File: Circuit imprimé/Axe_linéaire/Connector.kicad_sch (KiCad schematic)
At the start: 2 parts, among them J1 Conn_01x14_Shielded

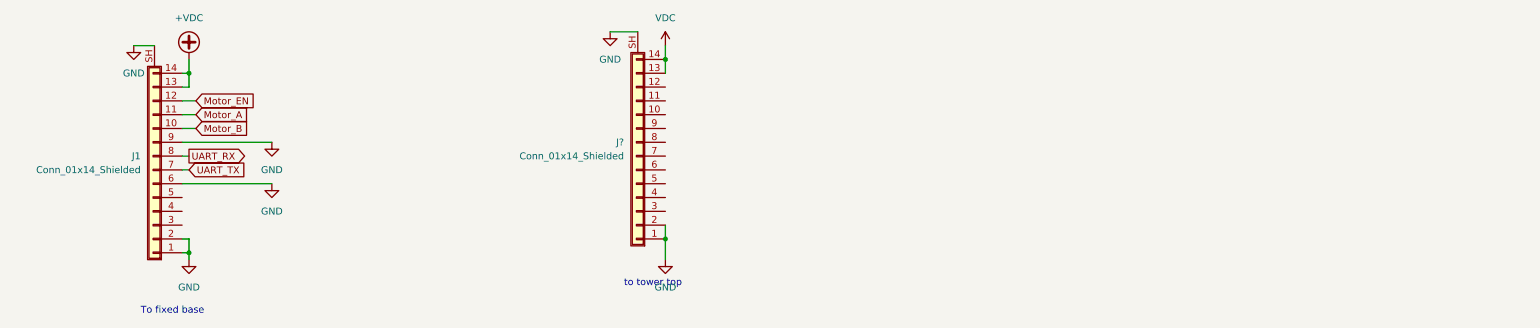
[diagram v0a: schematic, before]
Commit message: ajout du circuit de position + carte SD
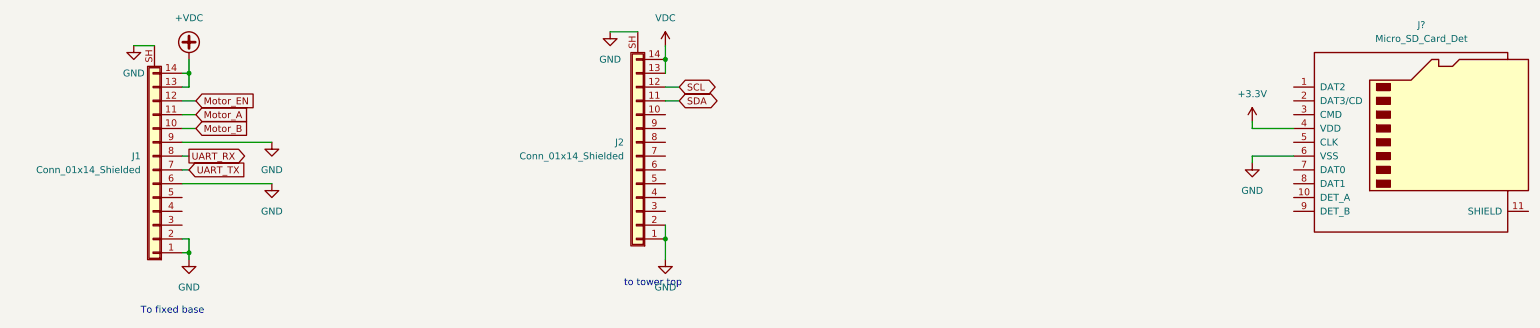
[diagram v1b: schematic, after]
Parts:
- added J?: Micro_SD_Card_Det, symbol Connector:Micro_SD_Card_Det
- gave numbers to parts that had none: 1
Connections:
- net GND: now also J?.6 (VSS)
- net SDA: now reaches J2.11 (Pin_11)
- net SCL: now reaches J2.12 (Pin_12)
- new net +3.3V: J?.4 (VDD)
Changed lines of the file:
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@@
+    (stroke (width 0) (type default) (color 0 0 0 0))
+  )
+  (wire (pts (xy 115.57 27.94) (xy 118.11 27.94))
+    (stroke (width 0) (type default) (color 0 0 0 0))
+  )
+  (wire (pts (xy 223.52 39.37) (xy 223.52 38.1))
     (stroke (width 0) (type default) (color 0 0 0 0))
   )
@@
     (stroke (width 0) (type default) (color 0 0 0 0))
   )
+  (wire (pts (xy 115.57 25.4) (xy 118.11 25.4))
+    (stroke (width 0) (type default) (color 0 0 0 0))
+  )
   (wire (pts (xy 26.67 30.48) (xy 29.21 30.48))
     (stroke (width 0) (type default) (color 0 0 0 0))
@@
     (stroke (width 0) (type default) (color 0 0 0 0))
   )
+  (wire (pts (xy 223.52 33.02) (xy 231.14 33.02))
+    (stroke (width 0) (type default) (color 0 0 0 0))
+  )
   (wire (pts (xy 26.67 22.86) (xy 27.94 22.86))
     (stroke (width 0) (type default) (color 0 0 0 0))
@@
     (stroke (width 0) (type default) (color 0 0 0 0))
   )
+  (wire (pts (xy 223.52 38.1) (xy 231.14 38.1))
+    (stroke (width 0) (type default) (color 0 0 0 0))
+  )
   (wire (pts (xy 115.57 20.32) (xy 115.57 22.86))
     (stroke (width 0) (type default) (color 0 0 0 0))
   )
   (wire (pts (xy 27.94 53.34) (xy 27.94 55.88))
+    (stroke (width 0) (type default) (color 0 0 0 0))
+  )
+  (wire (pts (xy 223.52 31.75) (xy 223.52 33.02))
     (stroke (width 0) (type default) (color 0 0 0 0))
   )
@@
     )
   )
+  (global_label "SCL" (shape bidirectional) (at 118.11 25.4 0) (fields_autoplaced)
+    (effects (font (size 1.27 1.27)) (justify left))
+    (property "Intersheet References" "${INTERSHEET_REFS}" (id 0) (at 124.0307 25.3206 0)
+      (effects (font (size 1.27 1.27)) (justify left) hide)
+    )
+  )
   (global_label "Motor_A" (shape input) (at 29.21 30.48 0) (fields_autoplaced)
     (effects (font (size 1.27 1.27)) (justify left))
@@
     (effects (font (size 1.27 1.27)) (justify left))
     (property "Intersheet References" "${INTERSHEET_REFS}" (id 0) (at 39.1221 32.9406 0)
+      (effects (font (size 1.27 1.27)) (justify left) hide)
+    )
+  )
+  (global_label "SDA" (shape bidirectional) (at 118.11 27.94 0) (fields_autoplaced)
+    (effects (font (size 1.27 1.27)) (justify left))
+    (property "Intersheet References" "${INTERSHEET_REFS}" (id 0) (at 124.0912 27.8606 0)
       (effects (font (size 1.27 1.27)) (justify left) hide)
     )
@@
   (symbol (lib_id "power:VDC") (at 115.57 17.78 0) (unit 1)
     (in_bom yes) (on_board yes) (fields_autoplaced)
-    (property "Reference" "#PWR?" (id 0) (at 115.57 20.32 0)
+    (property "Reference" "#PWR042" (id 0) (at 115.57 20.32 0)
       (effects (font (size 1.27 1.27)) hide)
     )
@@
   (symbol (lib_id "power:GND") (at 105.41 15.24 0) (unit 1)
     (in_bom yes) (on_board yes) (fields_autoplaced)
-    (property "Reference" "#PWR?" (id 0) (at 105.41 21.59 0)
+    (property "Reference" "#PWR041" (id 0) (at 105.41 21.59 0)
       (effects (font (size 1.27 1.27)) hide)
     )
@@
   (symbol (lib_id "power:GND") (at 115.57 57.15 0) (unit 1)
     (in_bom yes) (on_board yes) (fields_autoplaced)
-    (property "Reference" "#PWR?" (id 0) (at 115.57 63.5 0)
+    (property "Reference" "#PWR043" (id 0) (at 115.57 63.5 0)
       (effects (font (size 1.27 1.27)) hide)
     )
@@
   (symbol (lib_id "power:GND") (at 43.18 35.56 0) (unit 1)
     (in_bom yes) (on_board yes) (fields_autoplaced)
-    (property "Reference" "#PWR?" (id 0) (at 43.18 41.91 0)
+    (property "Reference" "#PWR039" (id 0) (at 43.18 41.91 0)
       (effects (font (size 1.27 1.27)) hide)
     )
@@
     )
     (pin "1")
+  )
+  (symbol (lib_id "Connector:Micro_SD_Card_Det") (at 254 35.56 0) (unit 1)
+    (in_bom yes) (on_board yes) (fields_autoplaced)
+    (property "Reference" "J?" (id 0) (at 254.635 13.97 0))
+    (property "Value" "Micro_SD_Card_Det" (id 1) (at 254.635 16.51 0))
+    (property "Footprint" "" (id 2) (at 306.07 17.78 0)
+      (effects (font (size 1.27 1.27)) hide)
+    )
+    (property "Datasheet" "https://www.hirose.com/product/en/download_file/key_name/DM3/category/Catalog/doc_file_id/49662/?file_category_id=4&item_id=195&is_series=1" (id 3) (at 254 33.02 0)
+      (effects (font (size 1.27 1.27)) hide)
+    )
+    (pin "1")
+    (pin "10")
+    (pin "11")
+    (pin "2")
+    (pin "3")
+    (pin "4")
+    (pin "5")
+    (pin "6")
+    (pin "7")
+    (pin "8")
+    (pin "9")
   )
   (symbol (lib_id "Connector_Generic_Shielded:Conn_01x14_Shielded") (at 21.59 40.64 180) (unit 1)
@@
     (pin "SH")
   )
+  (symbol (lib_id "power:+3.3V") (at 223.52 31.75 0) (unit 1)
+    (in_bom yes) (on_board yes) (fields_autoplaced)
+    (property "Reference" "#PWR?" (id 0) (at 223.52 35.56 0)
+      (effects (font (size 1.27 1.27)) hide)
+    )
+    (property "Value" "+3.3V" (id 1) (at 223.52 26.67 0))
+    (property "Footprint" "" (id 2) (at 223.52 31.75 0)
+      (effects (font (size 1.27 1.27)) hide)
+    )
+    (property "Datasheet" "" (id 3) (at 223.52 31.75 0)
+      (effects (font (size 1.27 1.27)) hide)
+    )
+    (pin "1")
+  )
   (symbol (lib_id "Connector_Generic_Shielded:Conn_01x14_Shielded") (at 110.49 38.1 180) (unit 1)
     (in_bom yes) (on_board yes) (fields_autoplaced)
-    (property "Reference" "J?" (id 0) (at 107.95 35.5599 0)
+    (property "Reference" "J2" (id 0) (at 107.95 35.5599 0)
       (effects (font (size 1.27 1.27)) (justify left))
     )
@@
   (symbol (lib_id "power:GND") (at 43.18 43.18 0) (unit 1)
     (in_bom yes) (on_board yes) (fields_autoplaced)
-    (property "Reference" "#PWR?" (id 0) (at 43.18 49.53 0)
+    (property "Reference" "#PWR040" (id 0) (at 43.18 49.53 0)
       (effects (font (size 1.27 1.27)) hide)
     )
@@
       (effects (font (size 1.27 1.27)) hide)
     )
+    (pin "1")
+  )
+  (symbol (lib_id "power:GND") (at 223.52 39.37 0) (unit 1)
+    (in_bom yes) (on_board yes) (fields_autoplaced)
+    (property "Reference" "#PWR?" (id 0) (at 223.52 45.72 0)
+      (effects (font (size 1.27 1.27)) hide)
+    )
+    (property "Value" "GND" (id 1) (at 223.52 44.45 0))
+    (property "Footprint" "" (id 2) (at 223.52 39.37 0)
+      (effects (font (size 1.27 1.27)) hide)
+    )
+    (property "Datasheet" "" (id 3) (at 223.52 39.37 0)
+      (effects (font (size 1.27 1.27)) hide)
+    )
